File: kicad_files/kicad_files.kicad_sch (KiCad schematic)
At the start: 6 parts, among them J1 Battery Connection, J2 Servo Connection, J3 DC Motor Connection, J4 Ultrasonic Sensor Connection, J5 Water Sensor Connection, J6 DC Motor Connection

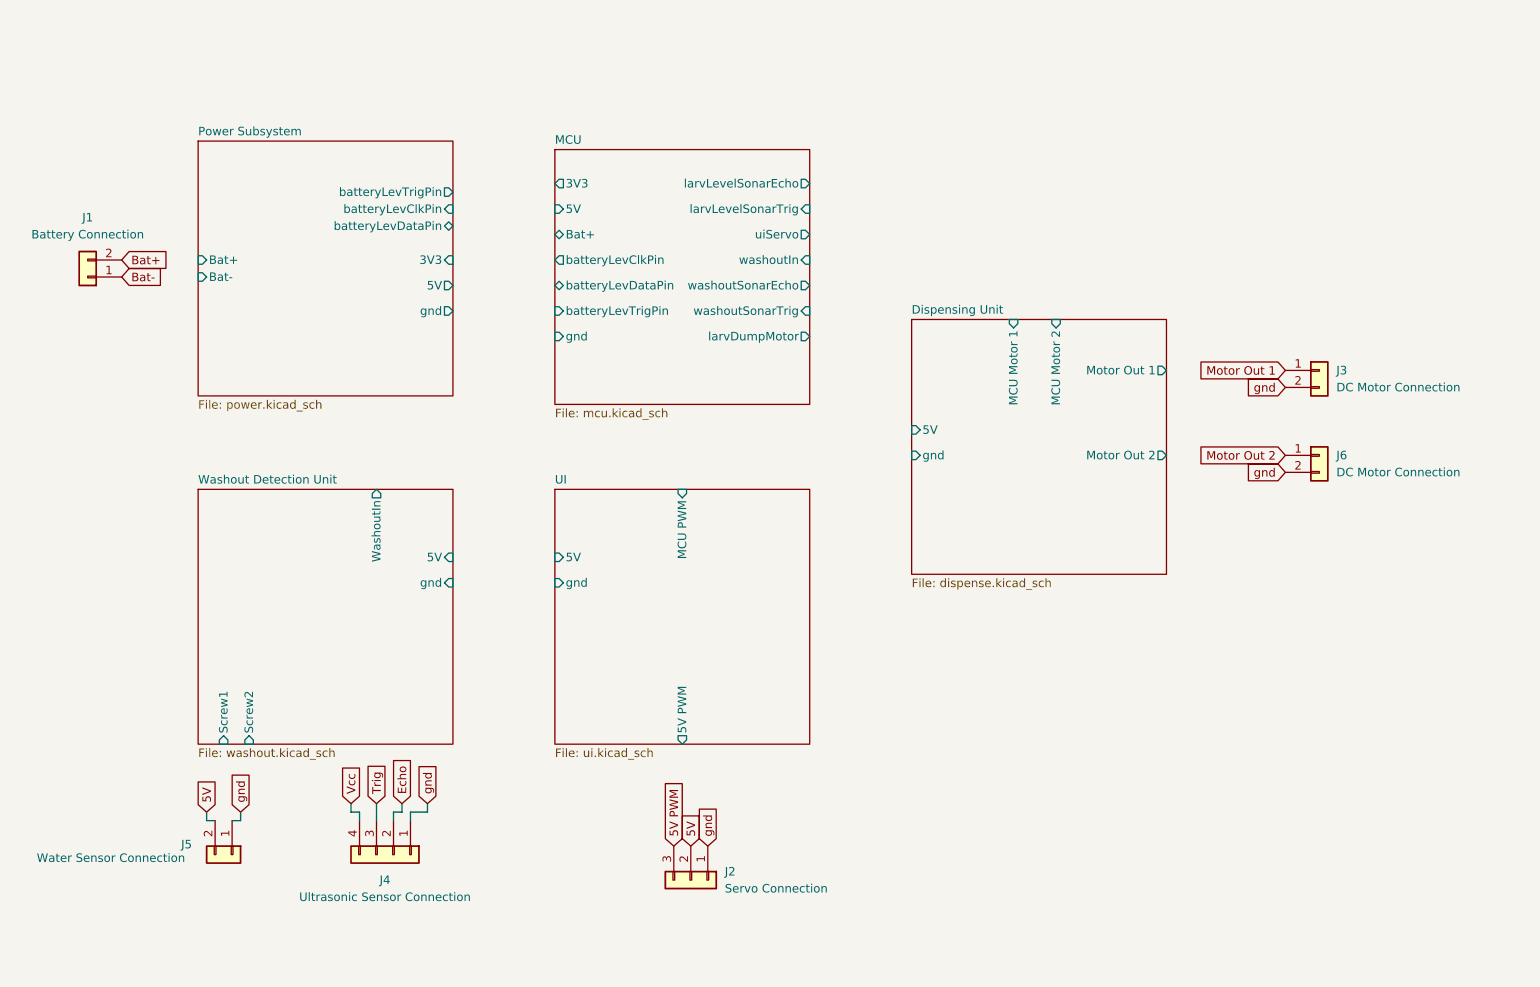
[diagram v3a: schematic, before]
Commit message: ERC errors cleaned. Hierarchical wiring finished. PWM converter change. Motor driver change.
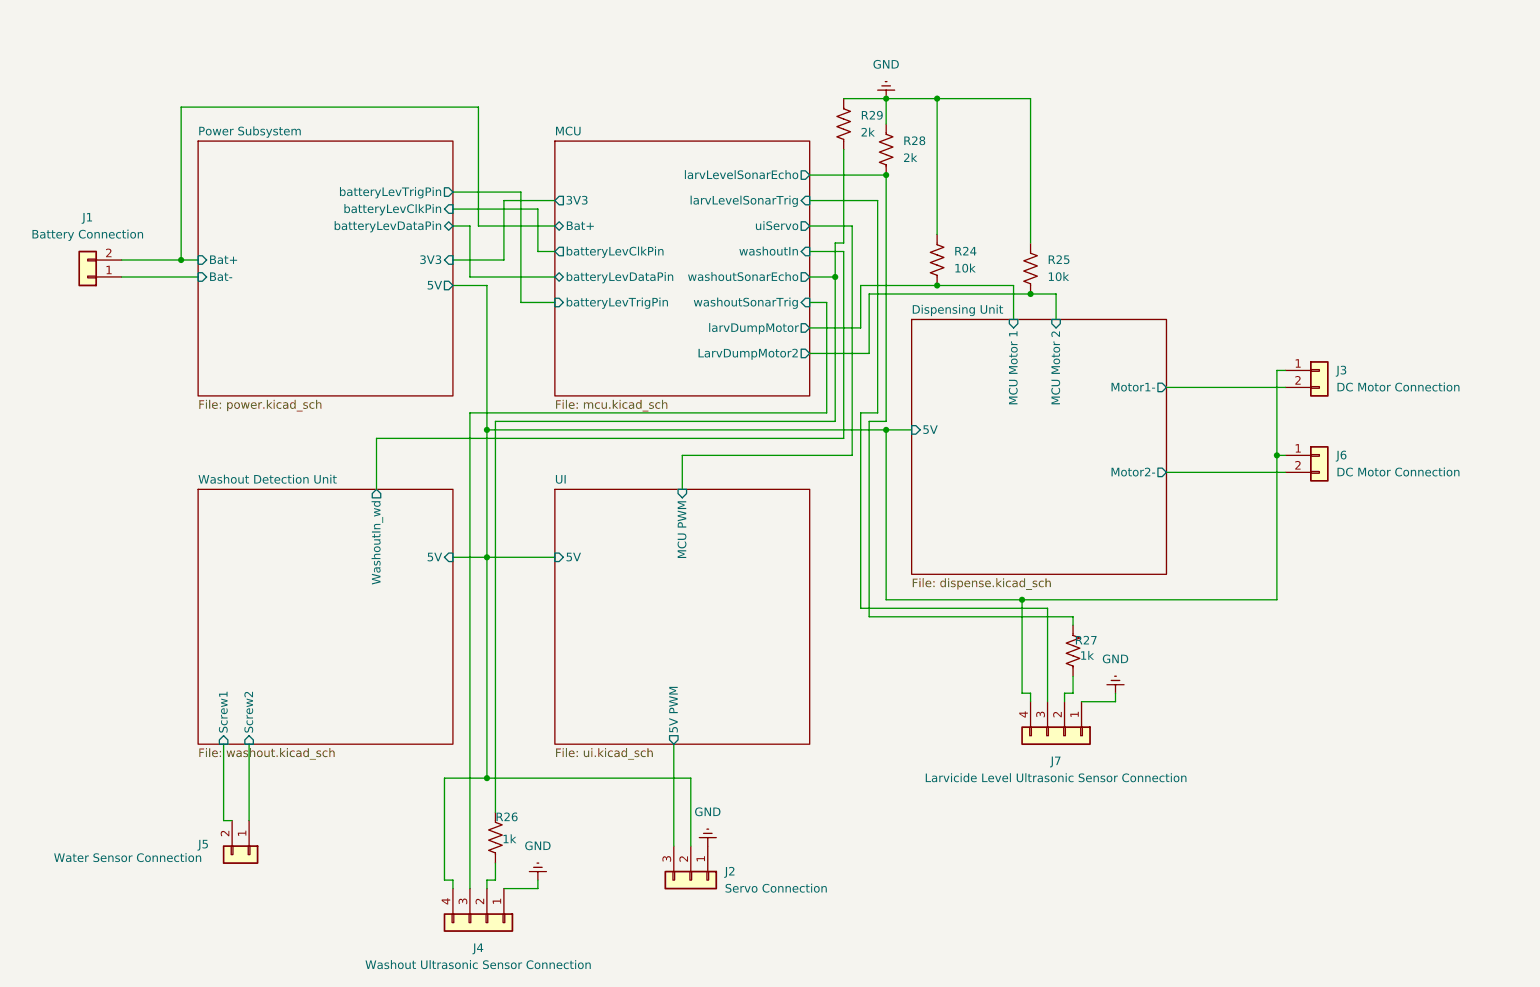
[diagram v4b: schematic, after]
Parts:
- added J7: Larvicide Level Ultrasonic Sensor Connection, symbol Connector_Generic:Conn_01x04
- added R24, R25: 10k, symbol Device:R_US
- added R26, R27: 1k, symbol Device:R_US
- added R28, R29: 2k, symbol Device:R_US
- J4: value Ultrasonic Sensor Connection -> Washout Ultrasonic Sensor Connection
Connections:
- net 5V PWM is gone; now on net UI/5V PWM: J2.3 (Pin_3)
- net Bat+ is gone; now on net MCU/Bat+: J1.2 (Pin_2)
- net Bat- is gone; now on net Power Subsystem/Bat-: J1.1 (Pin_1)
- net Motor Out 1 is gone; now on net Dispensing Unit/5V: J3.1 (Pin_1)
- net Motor Out 2 is gone; now on net Dispensing Unit/5V: J6.1 (Pin_1)
- net Trig is gone; now on net MCU/washoutSonarTrig: J4.3 (Pin_3)
- net Vcc is gone; now on net Dispensing Unit/5V: J4.4 (Pin_4)
- net Dispensing Unit/5V: now also J2.2 (Pin_2), J7.4 (Pin_4)
- net Dispensing Unit/MCU Motor 1: now also R24.2
- net Dispensing Unit/MCU Motor 2: now also R25.2
- net MCU/larvLevelSonarEcho: now also R27.1, R28.2
- net MCU/larvLevelSonarTrig: now also J7.3 (Pin_3)
- net MCU/washoutSonarEcho: now also R26.1, R29.2
- net Washout Detection Unit/Screw1: now also J5.2 (Pin_2)
- net Washout Detection Unit/Screw2: now also J5.1 (Pin_1)
- removed net 5V: J2.2 (Pin_2), J5.2 (Pin_2)
- net Echo: no longer names the net of J4.2 (Pin_2)
- net Echo: now also R26.2
- removed net gnd: J2.1 (Pin_1), J3.2 (Pin_2), J4.1 (Pin_1), J5.1 (Pin_1), J6.2 (Pin_2)
- new net: J7.2 (Pin_2), R27.2
- new net Dispensing Unit/Motor1-: J3.2 (Pin_2)
- new net Dispensing Unit/Motor2-: J6.2 (Pin_2)
- new net GND: J2.1 (Pin_1), J4.1 (Pin_1), J7.1 (Pin_1), R24.1, R25.1, R28.1, R29.1
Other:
- sheet Dispensing Unit ports: added Motor1-, Motor2-; removed Motor Out 1, Motor Out 2, gnd
- sheet MCU ports: added LarvDumpMotor2; removed 5V, gnd
- sheet Power Subsystem ports: added none; removed gnd
- sheet UI ports: added none; removed gnd
- sheet Washout Detection Unit ports: added WashoutIn_wd; removed WashoutIn, gnd
- moved on the sheet: J4, J5

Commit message: minor changes
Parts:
- removed J6: DC Motor Connection, symbol Connector_Generic:Conn_01x02
- removed R25: 10k, symbol Device:R_US
- added J6: Servo Connection, symbol Connector_Generic:Conn_01x03
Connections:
- net Dispensing Unit/5V: now also J6.2 (Pin_2)
- net GND: now also J6.1 (Pin_1)
- new net Dispensing Unit/5V PWM Dispense: J6.3 (Pin_3)
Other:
- sheet Dispensing Unit ports: added 5V PWM Dispense, MCU PWM Dispense; removed MCU Motor 2, Motor2-

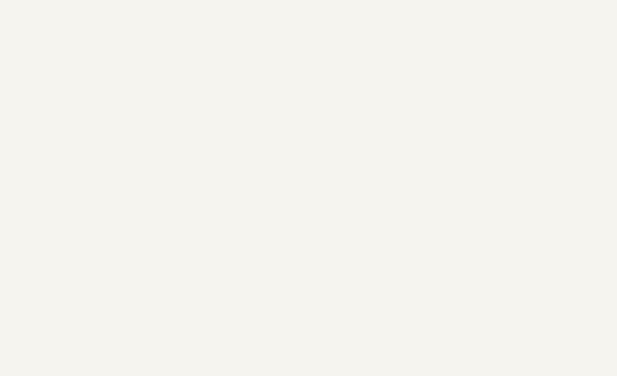
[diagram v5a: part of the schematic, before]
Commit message: Footprint assignment finished
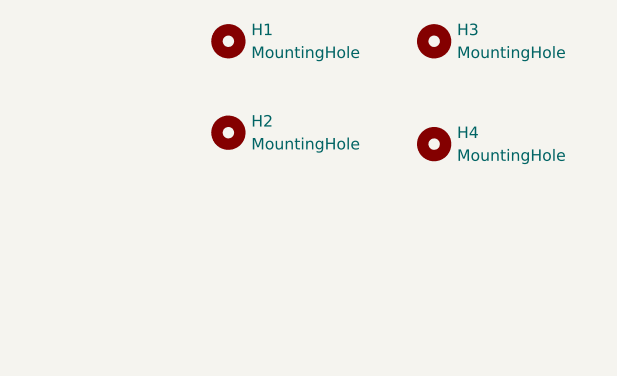
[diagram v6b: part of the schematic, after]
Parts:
- added H1, H2, H3, H4: MountingHole, MountingHole:MountingHole_3.2mm_M3, symbol Mechanical:MountingHole
- J1: footprint (none) -> Connector_JST:JST_VH_B2PS-VH_1x02_P3.96mm_Horizontal
- J2, J6: footprint (none) -> Connector_PinHeader_2.54mm:PinHeader_1x03_P2.54mm_Vertical
- J3, J5: footprint (none) -> Connector_JST:JST_XH_S2B-XH-A_1x02_P2.50mm_Horizontal
- J4, J7: footprint (none) -> Connector_JST:JST_XH_S4B-XH-A_1x04_P2.50mm_Horizontal
- R24, R26, R27, R28, R29: footprint (none) -> Resistor_SMD:R_1206_3216Metric_Pad1.30x1.75mm_HandSolder

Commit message: Housing and Dispensing Subsystem Models
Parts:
- J1: footprint Connector_JST:JST_VH_B2PS-VH_1x02_P3.96mm_Horizontal -> Connector_JST:JST_VH_B2P-VH_1x02_P3.96mm_Vertical
- J3, J5: footprint Connector_JST:JST_XH_S2B-XH-A_1x02_P2.50mm_Horizontal -> Connector_JST:JST_XH_B2B-XH-A_1x02_P2.50mm_Vertical
- J4, J7: footprint Connector_JST:JST_XH_S4B-XH-A_1x04_P2.50mm_Horizontal -> Connector_JST:JST_XH_B4B-XH-A_1x04_P2.50mm_Vertical
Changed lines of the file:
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@@
 			)
 		)
-		(property "Footprint" "Connector_JST:JST_XH_S4B-XH-A_1x04_P2.50mm_Horizontal"
+		(property "Footprint" "Connector_JST:JST_XH_B4B-XH-A_1x04_P2.50mm_Vertical"
 			(at 173.99 152.4 0)
 			(effects
@@
 			)
 		)
-		(property "Footprint" "Connector_JST:JST_XH_S2B-XH-A_1x02_P2.50mm_Horizontal"
+		(property "Footprint" "Connector_JST:JST_XH_B2B-XH-A_1x02_P2.50mm_Vertical"
 			(at 52.07 170.18 0)
 			(effects
@@
 			)
 		)
-		(property "Footprint" "Connector_JST:JST_VH_B2PS-VH_1x02_P3.96mm_Horizontal"
+		(property "Footprint" "Connector_JST:JST_VH_B2P-VH_1x02_P3.96mm_Vertical"
 			(at 27.94 83.82 0)
 			(effects
@@
 			)
 		)
-		(property "Footprint" "Connector_JST:JST_XH_S4B-XH-A_1x04_P2.50mm_Horizontal"
+		(property "Footprint" "Connector_JST:JST_XH_B4B-XH-A_1x04_P2.50mm_Vertical"
 			(at 87.63 180.34 0)
 			(effects
@@
 			)
 		)
-		(property "Footprint" "Connector_JST:JST_XH_S2B-XH-A_1x02_P2.50mm_Horizontal"
+		(property "Footprint" "Connector_JST:JST_XH_B2B-XH-A_1x02_P2.50mm_Vertical"
 			(at 212.09 97.79 0)
 			(effects

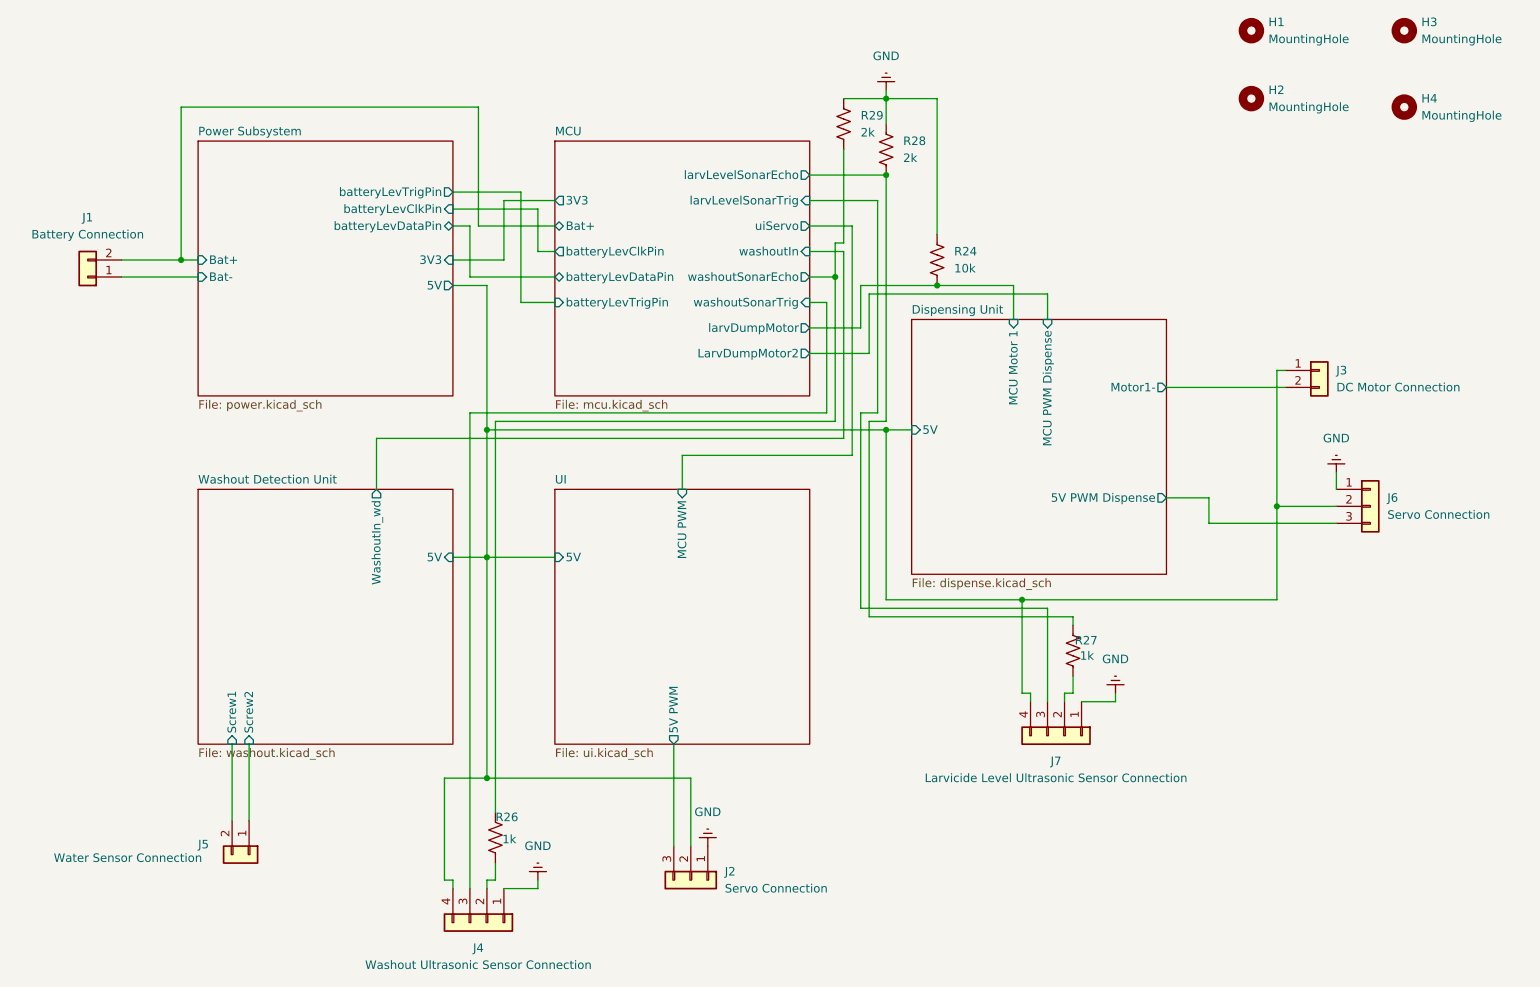
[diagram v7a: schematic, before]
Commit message: First pass floorplan and routing
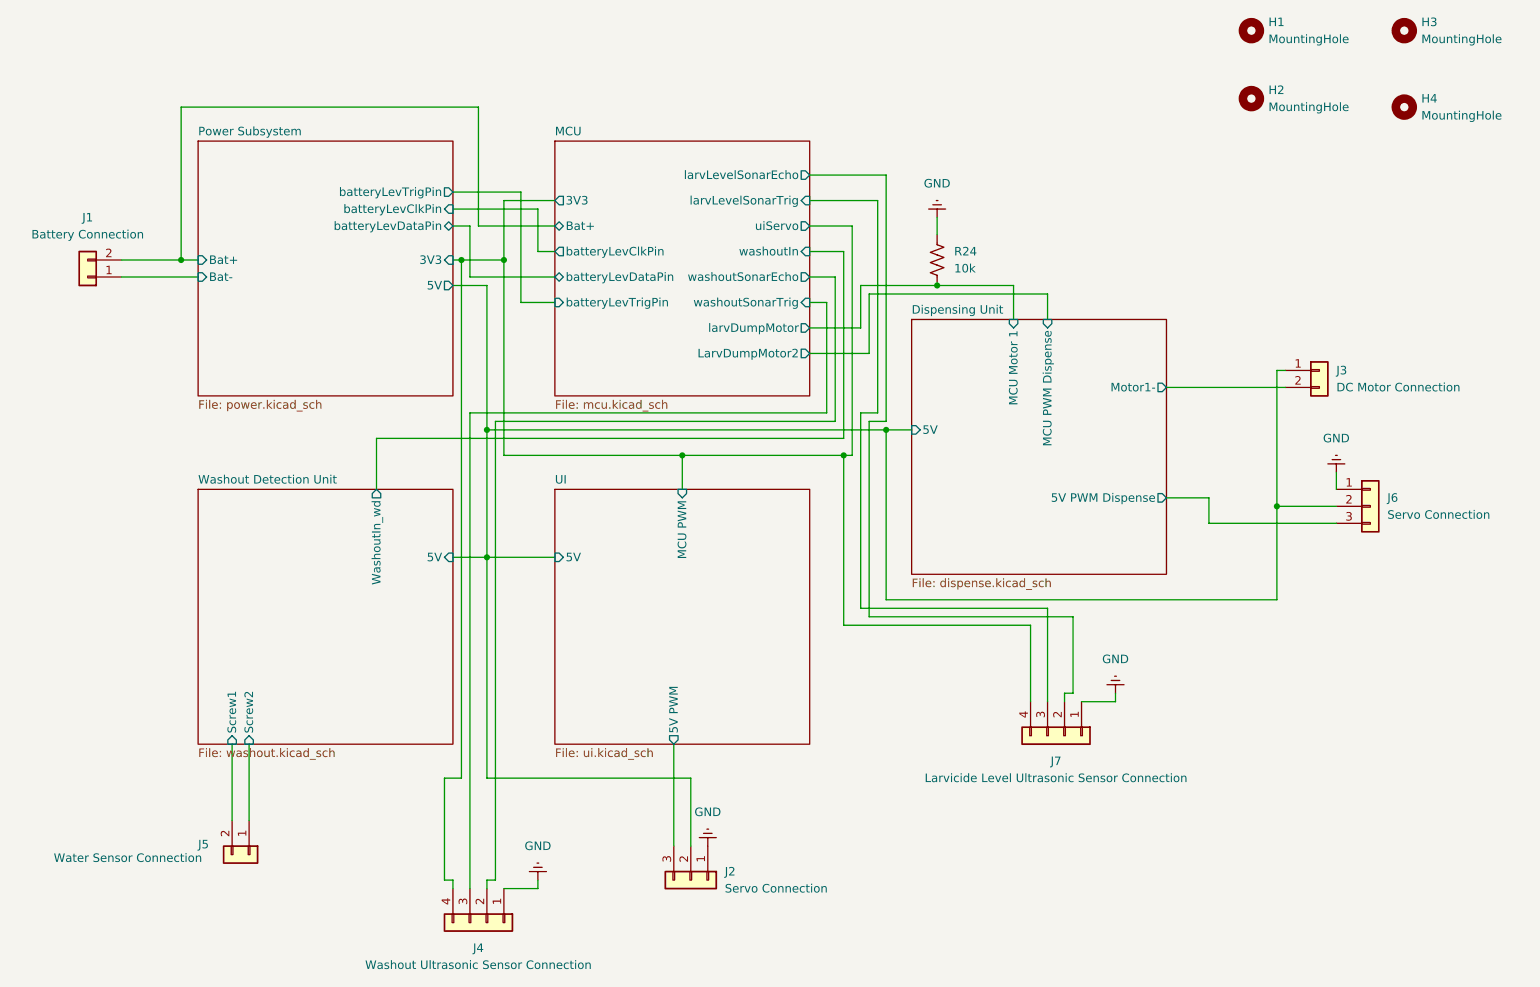
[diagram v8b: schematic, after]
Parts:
- removed R26, R27: 1k, Resistor_SMD:R_1206_3216Metric_Pad1.30x1.75mm_HandSolder, symbol Device:R_US
- removed R28, R29: 2k, Resistor_SMD:R_1206_3216Metric_Pad1.30x1.75mm_HandSolder, symbol Device:R_US
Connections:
- net Dispensing Unit/5V: no longer J4.4 (Pin_4), J7.4 (Pin_4)
- net MCU/3V3: now also J4.4 (Pin_4), J7.4 (Pin_4)
- net MCU/larvLevelSonarEcho: now also J7.2 (Pin_2)
- net MCU/washoutSonarEcho: now also J4.2 (Pin_2)
